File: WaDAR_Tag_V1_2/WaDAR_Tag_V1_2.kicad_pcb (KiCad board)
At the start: 2 copper layers, 34.6 x 30.7 mm, 11 parts, among them J1 SMA-J-P-H-RA-TH1, U1 SIT1569AC-J3-30E-0000.080000, U2 SKY13351-378LF

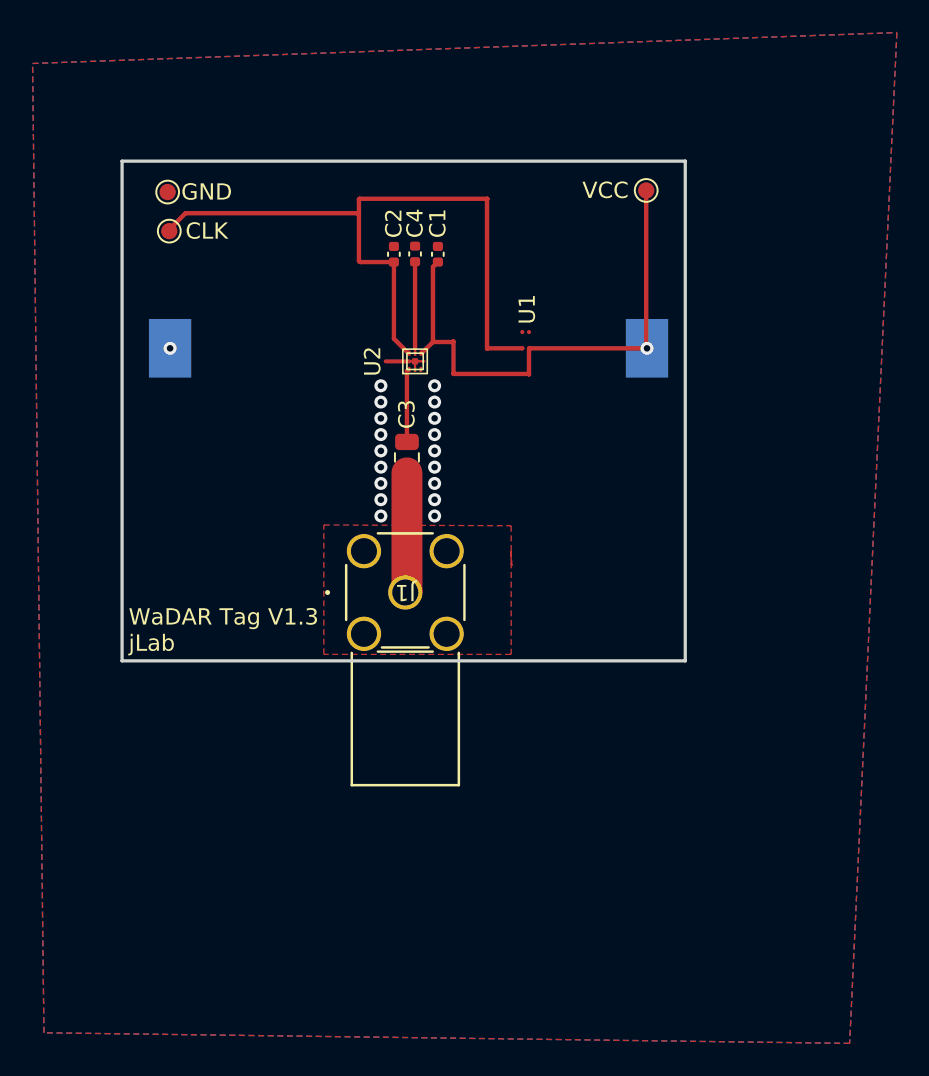
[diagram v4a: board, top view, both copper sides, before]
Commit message: updated capacitors and added mounting holes
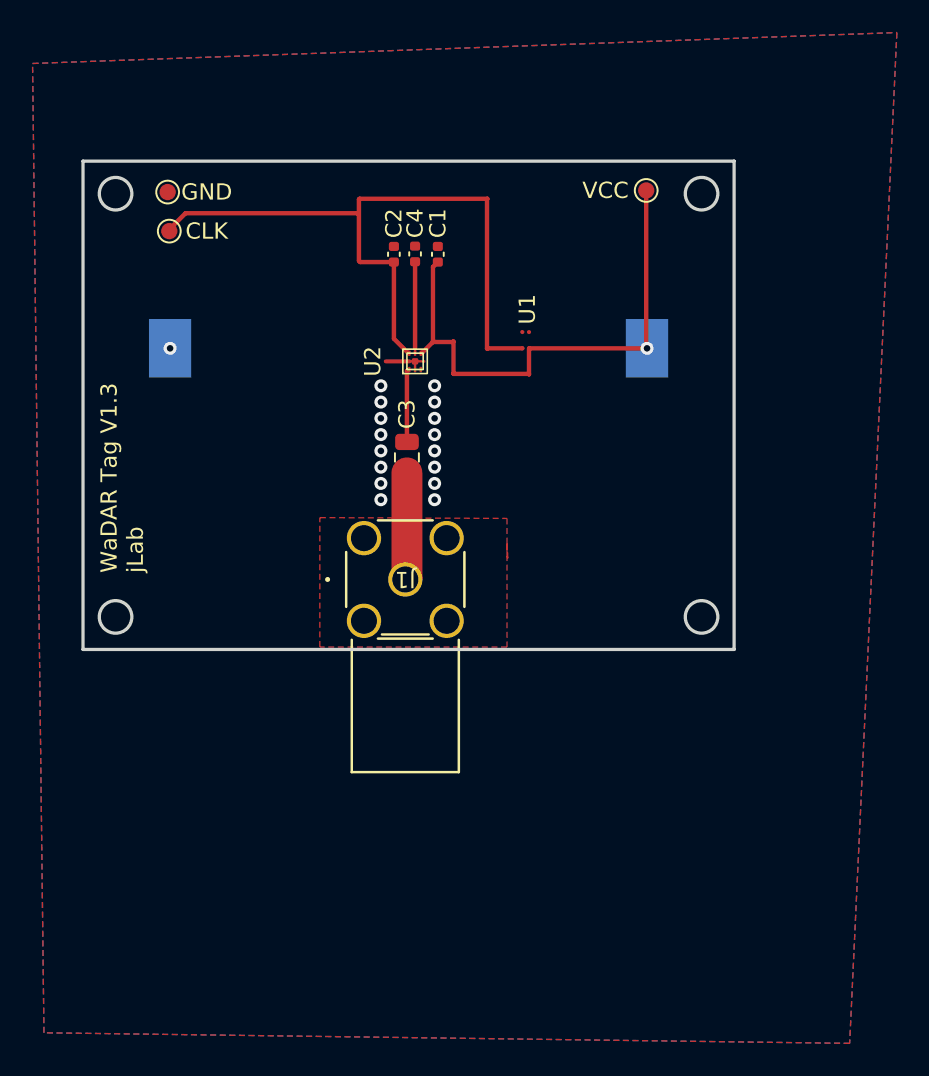
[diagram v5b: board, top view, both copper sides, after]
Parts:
- moved J1 0.80 mm to (163.4, 71.2)
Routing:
- net Net-(C3-Pad2): track 7.39 -> 6.59 mm
- net GND: vias 19 -> 17
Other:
- board size 34.6 x 30.7 mm -> 40 x 30 mm
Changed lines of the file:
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@@
 		(pad_to_mask_clearance 0)
 		(allow_soldermask_bridges_in_footprints no)
+		(grid_origin 143.6 45.5)
 		(pcbplotparams
 			(layerselection 0x00010fc_ffffffff)
@@
 	(footprint "WADARfootprints:CONN_SMA-J-P-H-RA-TH1_SAI"
 		(layer "F.Cu")
-		(at 163.4 72 180)
+		(at 163.4 71.2 180)
 		(tags "SMA-J-P-H-RA-TH1 ")
 		(property "Reference" "J1"
@@
 	)
 	(gr_rect
-		(start 146 45.5)
-		(end 180.6 76.2)
+		(start 143.6 45.5)
+		(end 183.6 75.5)
 		(stroke
 			(width 0.2)
@@
 		(layer "Edge.Cuts")
 	)
+	(gr_circle
+		(center 181.6 47.5)
+		(end 182.6 47.5)
+		(stroke
+			(width 0.2)
+			(type default)
+		)
+		(fill none)
+		(layer "Edge.Cuts")
+	)
+	(gr_circle
+		(center 145.6 73.5)
+		(end 146.6 73.5)
+		(stroke
+			(width 0.2)
+			(type default)
+		)
+		(fill none)
+		(layer "Edge.Cuts")
+	)
+	(gr_circle
+		(center 145.6 47.5)
+		(end 146.6 47.5)
+		(stroke
+			(width 0.2)
+			(type default)
+		)
+		(fill none)
+		(layer "Edge.Cuts")
+	)
+	(gr_circle
+		(center 181.6 73.5)
+		(end 182.6 73.5)
+		(stroke
+			(width 0.2)
+			(type default)
+		)
+		(fill none)
+		(layer "Edge.Cuts")
+	)
 	(gr_text "WaDAR Tag V1.3\njLab"
-		(at 146.4 75.7 0)
+		(at 147.4 70.8 90)
 		(layer "F.SilkS")
 		(effects
@@
 	)
 	(via
-		(at 165.2 67.3)
-		(size 0.8)
-		(drill 0.4)
-		(layers "F.Cu" "B.Cu")
-		(free yes)
-		(net 1)
-	)
-	(via
 		(at 161.9 64.3)
 		(size 0.8)
@@
 	)
 	(via
-		(at 161.9 67.3)
-		(size 0.8)
-		(drill 0.4)
-		(layers "F.Cu" "B.Cu")
-		(free yes)
-		(net 1)
-	)
-	(via
 		(at 161.9 59.3)
 		(size 0.8)
@@
 	)
 	(segment
+		(start 163.5 71.1)
+		(end 163.4 71.2)
+		(width 1.9)
+		(layer "F.Cu")
+		(net 4)
+	)
+	(segment
 		(start 163.5 64.65)
-		(end 163.5 71.9)
-		(width 1.9)
-		(layer "F.Cu")
-		(net 4)
-	)
-	(segment
-		(start 163.5 71.9)
-		(end 163.4 72)
+		(end 163.5 71.1)
 		(width 1.9)
 		(layer "F.Cu")
@@
 		(polygon
 			(pts
-				(xy 169.9 75.8) (xy 158.4 75.8) (xy 158.4 67.85) (xy 169.9 67.9) (xy 169.9 70.2) (xy 169.95 70.35)
-				(xy 169.9 69.45) (xy 169.9 70.15)
-			)
-		)
+				(xy 169.65 75.35) (xy 158.15 75.35) (xy 158.15 67.4) (xy 169.65 67.45) (xy 169.65 69.75) (xy 169.7 69.9)
+				(xy 169.65 69) (xy 169.65 69.7)
+			)
+		)

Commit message: V_2 off to assembly
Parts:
- added GND: GND, TestPoint:TestPoint_Pad_D1.0mm, F.Cu at (173.0, 47.3)
- C1, C2: value 33pF -> CAP CER 33PF 0402
- C3: value 100pF -> CAP CER 100PF 0805
- C4: value 100pF -> CAP CER 100PF 0402
- J1: value SMA-J-P-H-RA-TH1 -> 142-0701-321
- moved BT1 0.58 mm to (163.7, 56.4)
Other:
- board text added: "WaDAR Tag V1.2 jLab, EV"
- board text removed: "WaDAR Tag V1.3 jLab"
